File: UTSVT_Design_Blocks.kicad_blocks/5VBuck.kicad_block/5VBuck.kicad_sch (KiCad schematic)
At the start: 12 parts, among them U1 LMR51635XDDCR

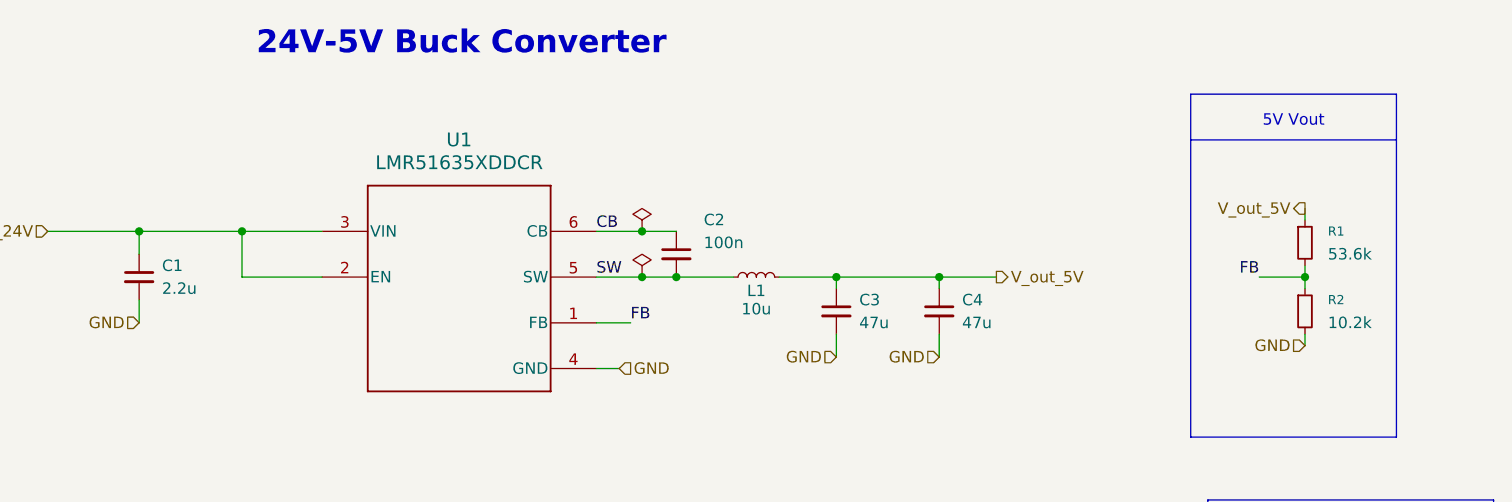
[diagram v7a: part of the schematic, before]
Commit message: updated 5V/12V buck capacitor footprint (#58)
* updated 5V buck capacitor footprint

* 12V Buck update for capacitor footprint to 0603
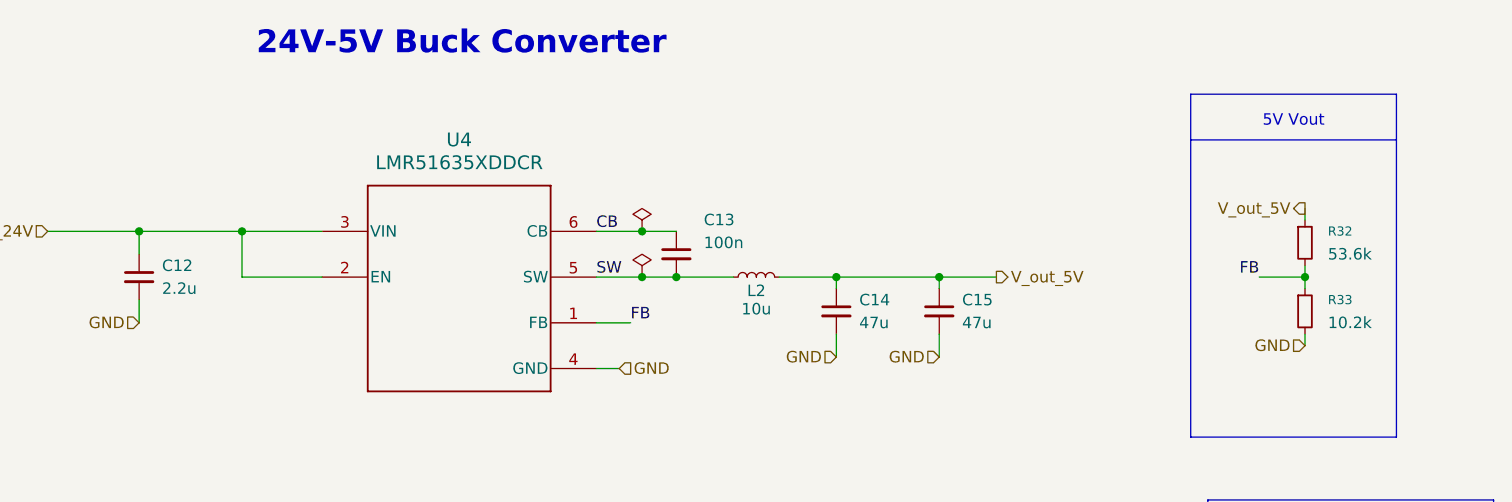
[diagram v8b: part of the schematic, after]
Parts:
- C13: renamed from C2; footprint Resistor_SMD:R_0201_0603Metric_Pad0.64x0.40mm_HandSolder -> Capacitor_SMD:C_0603_1608Metric
- TP13: renamed from TP5; footprint (none) -> TestPoint:TestPoint_THTPad_D3.0mm_Drill1.5mm
- TP14: renamed from TP7; footprint (none) -> TestPoint:TestPoint_THTPad_D3.0mm_Drill1.5mm
- TP15: renamed from TP6; footprint (none) -> TestPoint:TestPoint_THTPad_D3.0mm_Drill1.5mm
- TP16: renamed from TP8; footprint (none) -> TestPoint:TestPoint_THTPad_D3.0mm_Drill1.5mm
- renumbered C1 to C12, C3 to C14, C4 to C15, L1 to L2, R1 to R32, R2 to R33, U1 to U4
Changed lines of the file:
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@@
 		(on_board yes)
 		(dnp no)
-		(property "Reference" "L1"
+		(property "Reference" "L2"
 			(at 106.68 48.514 90)
 			(effects
@@
 			)
 			(project "5VBuck"
-				(path "/ad6c7df0-eb90-4670-9aa8-3e2007aefc2d/4ce3c563-64ba-4b6e-b334-e3956b5d5a33"
-					(reference "L1")
-					(unit 1)
-				)
-				(path "/ad6c7df0-eb90-4670-9aa8-3e2007aefc2d/c59a1097-f91e-4d56-b57d-869363ca5893"
-					(reference "L1")
+				(path "/ad6c7df0-eb90-4670-9aa8-3e2007aefc2d/ae63f0a9-78b8-4efb-b2ee-a2699a24d705"
+					(reference "L2")
 					(unit 1)
 				)
@@
 		(dnp no)
 		(fields_autoplaced yes)
-		(property "Reference" "R2"
+		(property "Reference" "R33"
 			(at 170.18 49.5299 0)
 			(effects
@@
 			)
 			(project "5VBuck"
-				(path "/ad6c7df0-eb90-4670-9aa8-3e2007aefc2d/4ce3c563-64ba-4b6e-b334-e3956b5d5a33"
-					(reference "R2")
-					(unit 1)
-				)
-				(path "/ad6c7df0-eb90-4670-9aa8-3e2007aefc2d/c59a1097-f91e-4d56-b57d-869363ca5893"
-					(reference "R2")
+				(path "/ad6c7df0-eb90-4670-9aa8-3e2007aefc2d/ae63f0a9-78b8-4efb-b2ee-a2699a24d705"
+					(reference "R33")
 					(unit 1)
 				)
@@
 		(dnp no)
 		(fields_autoplaced yes)
-		(property "Reference" "C1"
+		(property "Reference" "C12"
 			(at 40.64 45.7262 0)
 			(effects
@@
 			)
 			(project "5VBuck"
-				(path "/ad6c7df0-eb90-4670-9aa8-3e2007aefc2d/4ce3c563-64ba-4b6e-b334-e3956b5d5a33"
-					(reference "C1")
-					(unit 1)
-				)
-				(path "/ad6c7df0-eb90-4670-9aa8-3e2007aefc2d/c59a1097-f91e-4d56-b57d-869363ca5893"
-					(reference "C1")
+				(path "/ad6c7df0-eb90-4670-9aa8-3e2007aefc2d/ae63f0a9-78b8-4efb-b2ee-a2699a24d705"
+					(reference "C12")
 					(unit 1)
 				)
@@
 		(on_board yes)
 		(dnp no)
-		(property "Reference" "TP6"
+		(property "Reference" "TP15"
 			(at 184.15 80.5179 0)
 			(effects
@@
 			)
 		)
-		(property "Footprint" ""
+		(property "Footprint" "TestPoint:TestPoint_THTPad_D3.0mm_Drill1.5mm"
 			(at 186.69 85.09 0)
 			(effects
@@
 		(instances
 			(project "PowerPath"
-				(path "/ad6c7df0-eb90-4670-9aa8-3e2007aefc2d/4ce3c563-64ba-4b6e-b334-e3956b5d5a33"
-					(reference "TP6")
-					(unit 1)
-				)
-				(path "/ad6c7df0-eb90-4670-9aa8-3e2007aefc2d/c59a1097-f91e-4d56-b57d-869363ca5893"
-					(reference "TP6")
+				(path "/ad6c7df0-eb90-4670-9aa8-3e2007aefc2d/ae63f0a9-78b8-4efb-b2ee-a2699a24d705"
+					(reference "TP15")
 					(unit 1)
 				)
@@
 		(on_board yes)
 		(dnp no)
-		(property "Reference" "C2"
+		(property "Reference" "C13"
 			(at 100.838 40.64 0)
 			(effects
@@
 			)
 		)
-		(property "Footprint" "Resistor_SMD:R_0201_0603Metric_Pad0.64x0.40mm_HandSolder"
+		(property "Footprint" "Capacitor_SMD:C_0603_1608Metric"
 			(at 97.79 44.45 0)
 			(effects
@@
 			)
 			(project "5VBuck"
-				(path "/ad6c7df0-eb90-4670-9aa8-3e2007aefc2d/4ce3c563-64ba-4b6e-b334-e3956b5d5a33"
-					(reference "C2")
-					(unit 1)
-				)
-				(path "/ad6c7df0-eb90-4670-9aa8-3e2007aefc2d/c59a1097-f91e-4d56-b57d-869363ca5893"
-					(reference "C2")
+				(path "/ad6c7df0-eb90-4670-9aa8-3e2007aefc2d/ae63f0a9-78b8-4efb-b2ee-a2699a24d705"
+					(reference "C13")
 					(unit 1)
 				)
@@
 		(dnp no)
 		(fields_autoplaced yes)
-		(property "Reference" "U1"
+		(property "Reference" "U4"
 			(at 73.66 31.75 0)
 			(effects
@@
 			)
 			(project "5VBuck"
-				(path "/ad6c7df0-eb90-4670-9aa8-3e2007aefc2d/4ce3c563-64ba-4b6e-b334-e3956b5d5a33"
-					(reference "U1")
-					(unit 1)
-				)
-				(path "/ad6c7df0-eb90-4670-9aa8-3e2007aefc2d/c59a1097-f91e-4d56-b57d-869363ca5893"
-					(reference "U1")
+				(path "/ad6c7df0-eb90-4670-9aa8-3e2007aefc2d/ae63f0a9-78b8-4efb-b2ee-a2699a24d705"
+					(reference "U4")
 					(unit 1)
 				)
@@
 		(on_board yes)
 		(dnp no)
-		(property "Reference" "TP5"
+		(property "Reference" "TP13"
 			(at 171.45 80.5179 0)
 			(effects
@@
 			)
 		)
-		(property "Footprint" ""
+		(property "Footprint" "TestPoint:TestPoint_THTPad_D3.0mm_Drill1.5mm"
 			(at 173.99 85.09 0)
 			(effects
@@
 		(instances
 			(project ""
-				(path "/ad6c7df0-eb90-4670-9aa8-3e2007aefc2d/4ce3c563-64ba-4b6e-b334-e3956b5d5a33"
-					(reference "TP5")
-					(unit 1)
-				)
-				(path "/ad6c7df0-eb90-4670-9aa8-3e2007aefc2d/c59a1097-f91e-4d56-b57d-869363ca5893"
-					(reference "TP5")
+				(path "/ad6c7df0-eb90-4670-9aa8-3e2007aefc2d/ae63f0a9-78b8-4efb-b2ee-a2699a24d705"
+					(reference "TP13")
 					(unit 1)
 				)
@@
 		(dnp no)
 		(fields_autoplaced yes)
-		(property "Reference" "#FLG01"
+		(property "Reference" "#FLG010"
 			(at 93.98 40.005 0)
 			(effects
@@
 			)
 			(project "5VBuck"
-				(path "/ad6c7df0-eb90-4670-9aa8-3e2007aefc2d/4ce3c563-64ba-4b6e-b334-e3956b5d5a33"
-					(reference "#FLG01")
-					(unit 1)
-				)
-				(path "/ad6c7df0-eb90-4670-9aa8-3e2007aefc2d/c59a1097-f91e-4d56-b57d-869363ca5893"
-					(reference "#FLG01")
+				(path "/ad6c7df0-eb90-4670-9aa8-3e2007aefc2d/ae63f0a9-78b8-4efb-b2ee-a2699a24d705"
+					(reference "#FLG010")
 					(unit 1)
 				)
@@
 		(on_board yes)
 		(dnp no)
-		(property "Reference" "TP8"
+		(property "Reference" "TP16"
 			(at 184.15 93.2179 0)
 			(effects
@@
 			)
 		)
-		(property "Footprint" ""
+		(property "Footprint" "TestPoint:TestPoint_THTPad_D3.0mm_Drill1.5mm"
 			(at 186.69 97.79 0)
 			(effects
@@
 		(instances
 			(project "PowerPath"
-				(path "/ad6c7df0-eb90-4670-9aa8-3e2007aefc2d/4ce3c563-64ba-4b6e-b334-e3956b5d5a33"
-					(reference "TP8")
-					(unit 1)
-				)
-				(path "/ad6c7df0-eb90-4670-9aa8-3e2007aefc2d/c59a1097-f91e-4d56-b57d-869363ca5893"
-					(reference "TP8")
+				(path "/ad6c7df0-eb90-4670-9aa8-3e2007aefc2d/ae63f0a9-78b8-4efb-b2ee-a2699a24d705"
+					(reference "TP16")
 					(unit 1)
 				)
@@
 		(dnp no)
 		(fields_autoplaced yes)
-		(property "Reference" "C4"
+		(property "Reference" "C15"
 			(at 129.54 49.5362 0)
 			(effects
@@
 			)
 			(project "5VBuck"
-				(path "/ad6c7df0-eb90-4670-9aa8-3e2007aefc2d/4ce3c563-64ba-4b6e-b334-e3956b5d5a33"
-					(reference "C4")
-					(unit 1)
-				)
-				(path "/ad6c7df0-eb90-4670-9aa8-3e2007aefc2d/c59a1097-f91e-4d56-b57d-869363ca5893"
-					(reference "C4")
+				(path "/ad6c7df0-eb90-4670-9aa8-3e2007aefc2d/ae63f0a9-78b8-4efb-b2ee-a2699a24d705"
+					(reference "C15")
 					(unit 1)
 				)
@@
 		(on_board yes)
 		(dnp no)
-		(property "Reference" "#FLG02"
+		(property "Reference" "#FLG011"
 			(at 93.98 45.085 0)
 			(effects
@@
 			)
 			(project "5VBuck"
-				(path "/ad6c7df0-eb90-4670-9aa8-3e2007aefc2d/4ce3c563-64ba-4b6e-b334-e3956b5d5a33"
-					(reference "#FLG02")
-					(unit 1)
-				)
-				(path "/ad6c7df0-eb90-4670-9aa8-3e2007aefc2d/c59a1097-f91e-4d56-b57d-869363ca5893"
-					(reference "#FLG02")
+				(path "/ad6c7df0-eb90-4670-9aa8-3e2007aefc2d/ae63f0a9-78b8-4efb-b2ee-a2699a24d705"
+					(reference "#FLG011")
 					(unit 1)
 				)
@@
 		(dnp no)
 		(fields_autoplaced yes)
-		(property "Reference" "R1"
+		(property "Reference" "R32"
 			(at 170.18 41.9099 0)
 			(effects
@@
 			)
 			(project "5VBuck"
-				(path "/ad6c7df0-eb90-4670-9aa8-3e2007aefc2d/4ce3c563-64ba-4b6e-b334-e3956b5d5a33"
-					(reference "R1")
-					(unit 1)
-				)
-				(path "/ad6c7df0-eb90-4670-9aa8-3e2007aefc2d/c59a1097-f91e-4d56-b57d-869363ca5893"
-					(reference "R1")
+				(path "/ad6c7df0-eb90-4670-9aa8-3e2007aefc2d/ae63f0a9-78b8-4efb-b2ee-a2699a24d705"
+					(reference "R32")
 					(unit 1)
 				)
@@
 		(dnp no)
 		(fields_autoplaced yes)
-		(property "Reference" "C3"
+		(property "Reference" "C14"
 			(at 118.11 49.5362 0)
 			(effects
@@
 			)
 			(project "5VBuck"
-				(path "/ad6c7df0-eb90-4670-9aa8-3e2007aefc2d/4ce3c563-64ba-4b6e-b334-e3956b5d5a33"
-					(reference "C3")
-					(unit 1)
-				)
-				(path "/ad6c7df0-eb90-4670-9aa8-3e2007aefc2d/c59a1097-f91e-4d56-b57d-869363ca5893"
-					(reference "C3")
+				(path "/ad6c7df0-eb90-4670-9aa8-3e2007aefc2d/ae63f0a9-78b8-4efb-b2ee-a2699a24d705"
+					(reference "C14")
 					(unit 1)
 				)
@@
 		(on_board yes)
 		(dnp no)
-		(property "Reference" "TP7"
+		(property "Reference" "TP14"
 			(at 171.45 93.2179 0)
 			(effects
@@
 			)
 		)
-		(property "Footprint" ""
+		(property "Footprint" "TestPoint:TestPoint_THTPad_D3.0mm_Drill1.5mm"
 			(at 173.99 97.79 0)
 			(effects
@@
 		(instances
 			(project "PowerPath"
-				(path "/ad6c7df0-eb90-4670-9aa8-3e2007aefc2d/4ce3c563-64ba-4b6e-b334-e3956b5d5a33"
-					(reference "TP7")
-					(unit 1)
-				)
-				(path "/ad6c7df0-eb90-4670-9aa8-3e2007aefc2d/c59a1097-f91e-4d56-b57d-869363ca5893"
-					(reference "TP7")
-					(unit 1)
-				)
+				(path "/ad6c7df0-eb90-4670-9aa8-3e2007aefc2d/ae63f0a9-78b8-4efb-b2ee-a2699a24d705"
+					(reference "TP14")
+					(unit 1)
+				)
